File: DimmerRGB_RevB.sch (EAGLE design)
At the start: 54 parts, among them CON3 CON_10X200MIL, IC2 LM5111, IC3 LM2931_ADJ, IC4 LM5111, IC5 74HC14D, IC6 PIC16F18325, Q1 N-PWR-MOSFETLFPAK, Q2 N-PWR-MOSFETLFPAK, Q3 N-PWR-MOSFETLFPAK, Q4 N-PWR-MOSFETLFPAK, SW1 ENCODER_BOURNS, SW2 ENCODER_BOURNS, X1 22-23-2051

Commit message: Worked on RBG RevB layout
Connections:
- removed net N$16: R11.1, R12.1, SW2G$1.B, SW4G$1.B
- new net N$20: R11.1, R12.1, SW2G$1.B, SW4G$1.A
- net GND: now also SW3G$2.1, SW4G$2.1; no longer SW3G$2.2, SW4G$2.2
- net N$12: now also SW4G$2.2; no longer SW4G$2.1
- net N$13: now also SW3G$1.A; no longer SW3G$1.B
- net N$14: now also SW3G$1.B; no longer SW3G$1.A
- net N$17: now also SW4G$1.B; no longer SW4G$1.A
- net N$19: now also SW3G$2.2; no longer SW3G$2.1
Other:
- moved on the sheet: SW3, SW4
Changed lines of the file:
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@@
 <instance part="D4" gate="G$1" x="104.14" y="71.12"/>
 <instance part="SW3" gate="G$1" x="63.5" y="114.3"/>
-<instance part="SW3" gate="G$2" x="121.92" y="116.84" rot="R90"/>
+<instance part="SW3" gate="G$2" x="121.92" y="116.84" rot="R270"/>
 <instance part="SW4" gate="G$1" x="63.5" y="60.96"/>
-<instance part="SW4" gate="G$2" x="121.92" y="63.5" rot="R90"/>
+<instance part="SW4" gate="G$2" x="121.92" y="63.5" rot="R270"/>
 <instance part="GND37" gate="1" x="63.5" y="53.34"/>
 <instance part="GND38" gate="1" x="121.92" y="53.34"/>
@@
 </segment>
 <segment>
-<pinref part="SW4" gate="G$2" pin="2"/>
-<pinref part="GND38" gate="1" pin="GND"/>
-<wire x1="121.92" y1="58.42" x2="121.92" y2="55.88" width="0.1524" layer="91"/>
-</segment>
-<segment>
-<pinref part="SW3" gate="G$2" pin="2"/>
-<pinref part="GND39" gate="1" pin="GND"/>
-<wire x1="121.92" y1="111.76" x2="121.92" y2="109.22" width="0.1524" layer="91"/>
-</segment>
-<segment>
 <pinref part="SW3" gate="G$1" pin="C"/>
 <pinref part="GND40" gate="1" pin="GND"/>
 <wire x1="63.5" y1="111.76" x2="63.5" y2="109.22" width="0.1524" layer="91"/>
+</segment>
+<segment>
+<pinref part="SW4" gate="G$2" pin="1"/>
+<pinref part="GND38" gate="1" pin="GND"/>
+<wire x1="121.92" y1="58.42" x2="121.92" y2="55.88" width="0.1524" layer="91"/>
+</segment>
+<segment>
+<pinref part="SW3" gate="G$2" pin="1"/>
+<pinref part="GND39" gate="1" pin="GND"/>
+<wire x1="121.92" y1="111.76" x2="121.92" y2="109.22" width="0.1524" layer="91"/>
 </segment>
 </net>
@@
 <wire x1="55.88" y1="137.16" x2="55.88" y2="134.62" width="0.1524" layer="91"/>
 <pinref part="R6" gate="G$1" pin="1"/>
-<wire x1="55.88" y1="134.62" x2="55.88" y2="127" width="0.1524" layer="91"/>
-<wire x1="55.88" y1="127" x2="55.88" y2="121.92" width="0.1524" layer="91"/>
+<wire x1="55.88" y1="134.62" x2="55.88" y2="124.46" width="0.1524" layer="91"/>
+<wire x1="55.88" y1="124.46" x2="55.88" y2="121.92" width="0.1524" layer="91"/>
 <wire x1="58.42" y1="134.62" x2="55.88" y2="134.62" width="0.1524" layer="91"/>
 <junction x="55.88" y="134.62"/>
-<pinref part="SW3" gate="G$1" pin="B"/>
-<wire x1="55.88" y1="127" x2="66.04" y2="127" width="0.1524" layer="91"/>
-<wire x1="66.04" y1="127" x2="66.04" y2="121.92" width="0.1524" layer="91"/>
-<junction x="55.88" y="127"/>
+<pinref part="SW3" gate="G$1" pin="A"/>
+<wire x1="60.96" y1="121.92" x2="60.96" y2="124.46" width="0.1524" layer="91"/>
+<wire x1="60.96" y1="124.46" x2="55.88" y2="124.46" width="0.1524" layer="91"/>
+<junction x="55.88" y="124.46"/>
 </segment>
 </net>
@@
 <wire x1="50.8" y1="137.16" x2="50.8" y2="134.62" width="0.1524" layer="91"/>
 <pinref part="R2" gate="G$1" pin="2"/>
-<wire x1="50.8" y1="134.62" x2="50.8" y2="124.46" width="0.1524" layer="91"/>
-<wire x1="50.8" y1="124.46" x2="50.8" y2="121.92" width="0.1524" layer="91"/>
+<wire x1="50.8" y1="134.62" x2="50.8" y2="127" width="0.1524" layer="91"/>
+<wire x1="50.8" y1="127" x2="50.8" y2="121.92" width="0.1524" layer="91"/>
 <wire x1="48.26" y1="134.62" x2="50.8" y2="134.62" width="0.1524" layer="91"/>
 <junction x="50.8" y="134.62"/>
-<pinref part="SW3" gate="G$1" pin="A"/>
-<wire x1="50.8" y1="124.46" x2="60.96" y2="124.46" width="0.1524" layer="91"/>
-<wire x1="60.96" y1="124.46" x2="60.96" y2="121.92" width="0.1524" layer="91"/>
-<junction x="50.8" y="124.46"/>
+<pinref part="SW3" gate="G$1" pin="B"/>
+<wire x1="50.8" y1="127" x2="66.04" y2="127" width="0.1524" layer="91"/>
+<wire x1="66.04" y1="127" x2="66.04" y2="121.92" width="0.1524" layer="91"/>
+<junction x="50.8" y="127"/>
 </segment>
 </net>
@@
 <wire x1="182.88" y1="73.66" x2="172.72" y2="73.66" width="0.1524" layer="91"/>
 <label x="172.72" y="73.66" size="1.778" layer="95"/>
-</segment>
-</net>
-<net name="N$16" class="0">
-<segment>
-<pinref part="R11" gate="G$1" pin="1"/>
-<pinref part="SW2" gate="G$1" pin="B"/>
-<wire x1="55.88" y1="83.82" x2="55.88" y2="81.28" width="0.1524" layer="91"/>
-<pinref part="R12" gate="G$1" pin="1"/>
-<wire x1="55.88" y1="81.28" x2="55.88" y2="73.66" width="0.1524" layer="91"/>
-<wire x1="55.88" y1="73.66" x2="55.88" y2="68.58" width="0.1524" layer="91"/>
-<wire x1="58.42" y1="81.28" x2="55.88" y2="81.28" width="0.1524" layer="91"/>
-<junction x="55.88" y="81.28"/>
-<pinref part="SW4" gate="G$1" pin="B"/>
-<wire x1="66.04" y1="68.58" x2="66.04" y2="73.66" width="0.1524" layer="91"/>
-<wire x1="66.04" y1="73.66" x2="55.88" y2="73.66" width="0.1524" layer="91"/>
-<junction x="55.88" y="73.66"/>
-</segment>
-</net>
-<net name="N$17" class="0">
-<segment>
-<pinref part="R9" gate="G$1" pin="1"/>
-<pinref part="SW2" gate="G$1" pin="A"/>
-<wire x1="50.8" y1="83.82" x2="50.8" y2="81.28" width="0.1524" layer="91"/>
-<pinref part="R10" gate="G$1" pin="2"/>
-<wire x1="50.8" y1="81.28" x2="50.8" y2="71.12" width="0.1524" layer="91"/>
-<wire x1="50.8" y1="71.12" x2="50.8" y2="68.58" width="0.1524" layer="91"/>
-<wire x1="48.26" y1="81.28" x2="50.8" y2="81.28" width="0.1524" layer="91"/>
-<junction x="50.8" y="81.28"/>
-<pinref part="SW4" gate="G$1" pin="A"/>
-<wire x1="60.96" y1="68.58" x2="60.96" y2="71.12" width="0.1524" layer="91"/>
-<wire x1="60.96" y1="71.12" x2="50.8" y2="71.12" width="0.1524" layer="91"/>
-<junction x="50.8" y="71.12"/>
 </segment>
 </net>
@@
 <wire x1="114.3" y1="71.12" x2="106.68" y2="71.12" width="0.1524" layer="91"/>
 <junction x="114.3" y="71.12"/>
-<pinref part="SW4" gate="G$2" pin="1"/>
 <wire x1="114.3" y1="71.12" x2="121.92" y2="71.12" width="0.1524" layer="91"/>
+<pinref part="SW4" gate="G$2" pin="2"/>
 <wire x1="121.92" y1="71.12" x2="121.92" y2="68.58" width="0.1524" layer="91"/>
 </segment>
@@
 <wire x1="106.68" y1="124.46" x2="114.3" y2="124.46" width="0.1524" layer="91"/>
 <junction x="114.3" y="124.46"/>
-<pinref part="SW3" gate="G$2" pin="1"/>
 <wire x1="114.3" y1="124.46" x2="121.92" y2="124.46" width="0.1524" layer="91"/>
-<wire x1="121.92" y1="124.46" x2="121.92" y2="121.92" width="0.1524" layer="91"/>
-</segment>
-</net>
+<pinref part="SW3" gate="G$2" pin="2"/>
+<wire x1="121.92" y1="121.92" x2="121.92" y2="124.46" width="0.1524" layer="91"/>
+</segment>
+</net>
+<net name="N$20" class="0">
+<segment>
+<pinref part="SW4" gate="G$1" pin="A"/>
+<wire x1="60.96" y1="68.58" x2="60.96" y2="71.12" width="0.1524" layer="91"/>
+<pinref part="R11" gate="G$1" pin="1"/>
+<pinref part="SW2" gate="G$1" pin="B"/>
+<wire x1="55.88" y1="83.82" x2="55.88" y2="81.28" width="0.1524" layer="91"/>
+<pinref part="R12" gate="G$1" pin="1"/>
+<wire x1="55.88" y1="81.28" x2="55.88" y2="71.12" width="0.1524" layer="91"/>
+<wire x1="55.88" y1="71.12" x2="55.88" y2="68.58" width="0.1524" layer="91"/>
+<wire x1="58.42" y1="81.28" x2="55.88" y2="81.28" width="0.1524" layer="91"/>
+<junction x="55.88" y="81.28"/>
+<wire x1="60.96" y1="71.12" x2="55.88" y2="71.12" width="0.1524" layer="91"/>
+<junction x="55.88" y="71.12"/>
+</segment>
+</net>
+<net name="N$17" class="0">
+<segment>
+<pinref part="SW4" gate="G$1" pin="B"/>
+<wire x1="66.04" y1="68.58" x2="66.04" y2="73.66" width="0.1524" layer="91"/>
+<pinref part="R9" gate="G$1" pin="1"/>
+<pinref part="SW2" gate="G$1" pin="A"/>
+<wire x1="50.8" y1="83.82" x2="50.8" y2="81.28" width="0.1524" layer="91"/>
+<pinref part="R10" gate="G$1" pin="2"/>
+<wire x1="50.8" y1="81.28" x2="50.8" y2="73.66" width="0.1524" layer="91"/>
+<wire x1="50.8" y1="73.66" x2="50.8" y2="68.58" width="0.1524" layer="91"/>
+<wire x1="48.26" y1="81.28" x2="50.8" y2="81.28" width="0.1524" layer="91"/>
+<junction x="50.8" y="81.28"/>
+<wire x1="66.04" y1="73.66" x2="50.8" y2="73.66" width="0.1524" layer="91"/>
+<junction x="50.8" y="73.66"/>
+</segment>
+</net>

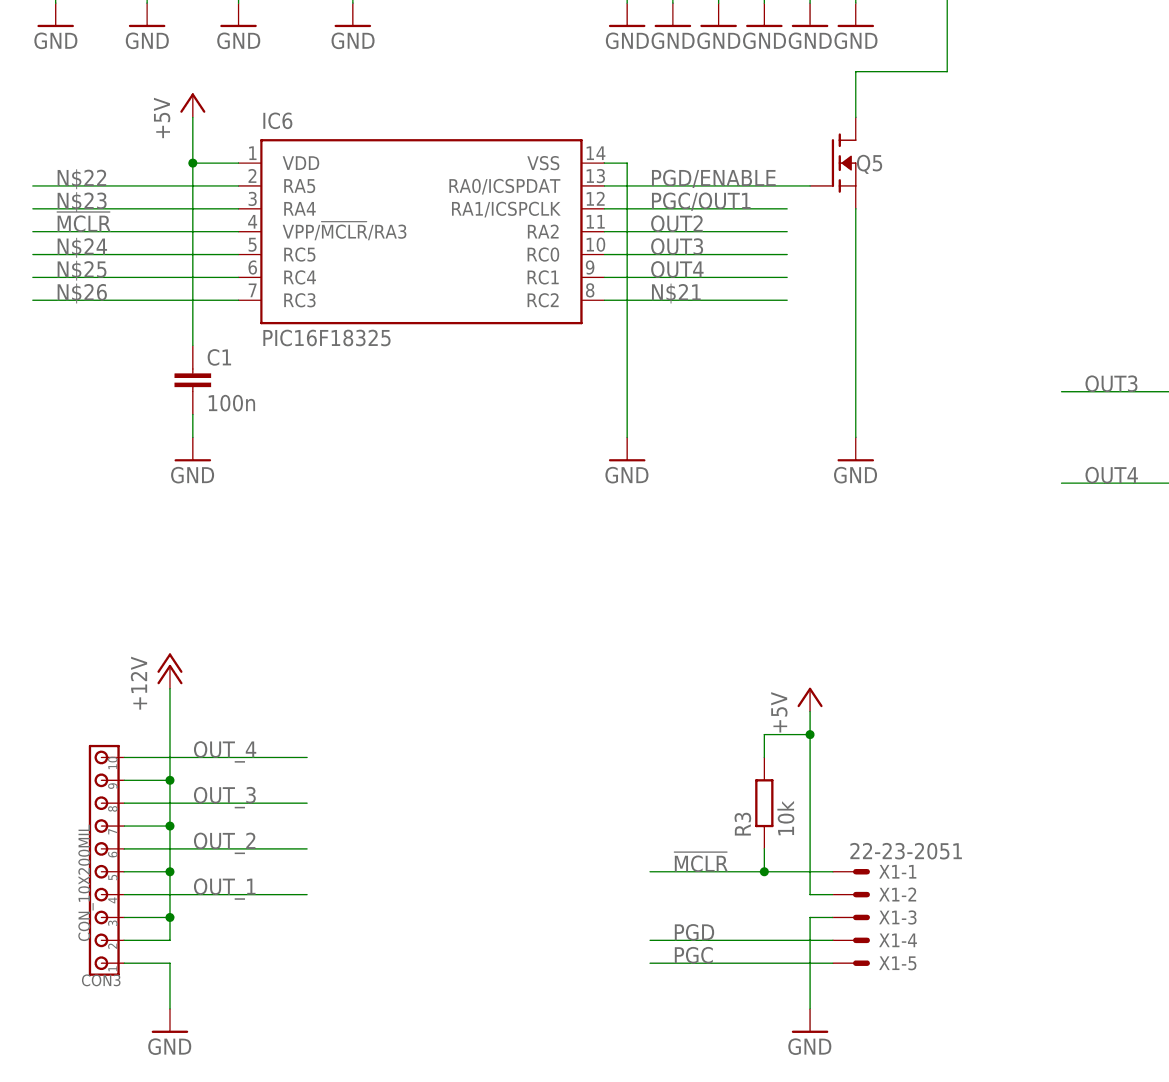
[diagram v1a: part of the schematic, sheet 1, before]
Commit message: Some more layouting done
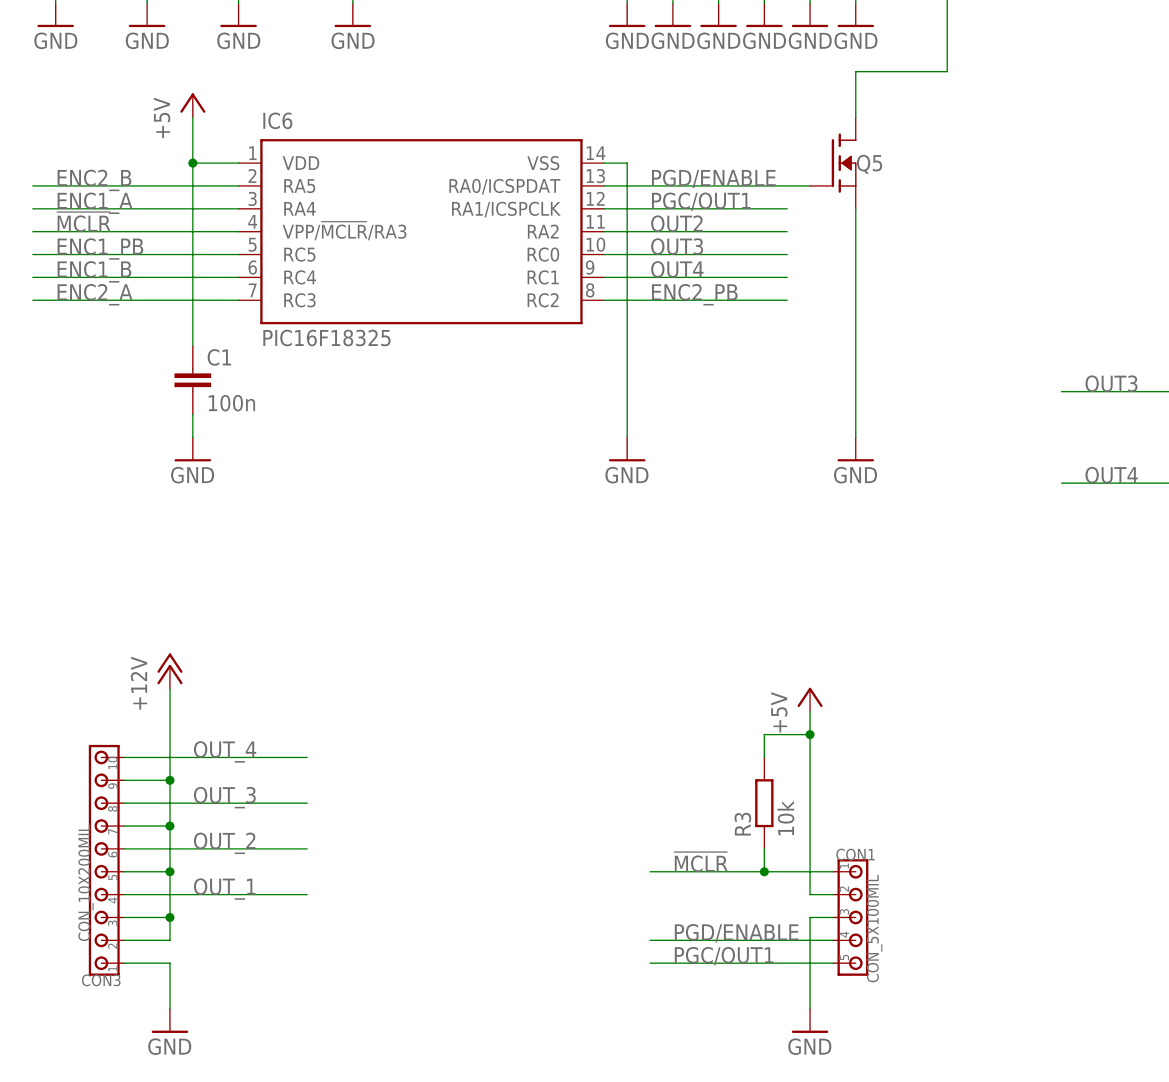
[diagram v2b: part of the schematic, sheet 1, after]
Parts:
- removed X1: 22-23-2051, 00Connector:22-23-2051
- added CON1: CON_5X100MIL, 00Connector:CON_5X100MIL
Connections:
- removed net N$21: IC6.RC2
- removed net N$22: IC6.RA5
- removed net N$23: IC6.RA4
- removed net N$24: IC6.RC5
- removed net N$25: IC6.RC4
- removed net N$26: IC6.RC3
- removed net PGC: X1-5.S
- removed net PGD: X1-4.S
- net !MCLR!: now also CON1.1; no longer X1-1.S
- net +5V: now also CON1.2; no longer X1-2.S
- net ENC1A: now also IC5.5A; no longer IC5.2A
- net ENC1B: now also IC5.6A; no longer IC5.3A
- net ENC1PB: now also IC5.4A; no longer IC5.1A
- net ENC1_A: now also IC5.5Y, IC6.RA4; no longer IC5.2Y
- net ENC1_B: now also IC5.6Y, IC6.RC4; no longer IC5.3Y
- net ENC1_PB: now also IC5.4Y, IC6.RC5; no longer IC5.1Y
- net ENC2A: now also IC5.1A; no longer IC5.5A
- net ENC2B: now also IC5.2A; no longer IC5.6A
- net ENC2PB: now also IC5.3A; no longer IC5.4A
- net ENC2_A: now also IC5.1Y, IC6.RC3; no longer IC5.5Y
- net ENC2_B: now also IC5.2Y, IC6.RA5; no longer IC5.6Y
- net ENC2_PB: now also IC5.3Y, IC6.RC2; no longer IC5.4Y
- net GND: now also CON1.3; no longer X1-3.S
- net PGC/OUT1: now also CON1.5
- net PGD/ENABLE: now also CON1.4

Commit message: Final version of RGB dimmer Rev B
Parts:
- removed CON3: CON_10X200MIL, 00Connector:CON_10X200MIL
- added C19, C20, C21, C22, C23, C8: 100n, 00Capacitor:CC0805
- added C7: 1500u, 00Capacitor:C_POLARIZED10MM
- added CON2: CON_5X100MIL, 00Connector:CON_5X100MIL
- C1: value 100n -> 33u; device 00Capacitor:CC0805 -> 00Capacitor:C_POLARIZEDSMC_C
- C11, C12: value 10n -> 100n
- C13, C14: value 100n -> 10n
- C17, C18, C2: value 1500u -> 100n; device 00Capacitor:C_POLARIZED10MM -> 00Capacitor:CC0805
- C3: value 33u -> 1500u; device 00Capacitor:C_POLARIZEDSMC_C -> 00Capacitor:C_POLARIZED10MM
- C6: value 100n -> 1500u; device 00Capacitor:CC0805 -> 00Capacitor:C_POLARIZED10MM
- CON1: value CON_5X100MIL -> CON_10X200MIL; device 00Connector:CON_5X100MIL -> 00Connector:CON_10X200MIL
- IC2: value LM5111 -> LM2931_ADJ; device 00Logic:LM5111 -> 00VoltageRegulator:LM2931_ADJ
- IC3: value LM2931_ADJ -> LM5111; device 00VoltageRegulator:LM2931_ADJ -> 00Logic:LM5111
- Q1: value N-PWR-MOSFETLFPAK -> (none); device 00Mosfet:N-PWR-MOSFETLFPAK -> 00Mosfet:N-FETSOT23
- Q5: value (none) -> N-PWR-MOSFETLFPAK; device 00Mosfet:N-FETSOT23 -> 00Mosfet:N-PWR-MOSFETLFPAK
- R1: value 10k -> 1k
- R10, R14, R8: value 22k -> 10k
- R13, R17, R7: value 10k -> 22k
- R15: value 33k -> 10k
- R16: value 33k -> 22k
- R2: value 22k -> 33k
- R4: value 1k -> 10k
- R5: value 10k -> 33k
- SW1, SW2: value ENCODER_BOURNS -> PEC11R
- SW3, SW4: value (none) -> PEC09
- renumbered IC6 to IC1
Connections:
- removed net N$6 (its old number): IC2.OUT_A, Q2.G
- new net N$5: IC3.OUT_A, Q2.G
- net !ENABLE!: now also D1.A, IC2.!EN!, Q1.D, R5.1; no longer D4.A, IC3.!EN!, Q5.D, R15.1
- net !MCLR!: now also CON2.1, R4.1; no longer CON1.1, R3.1
- net +12V: now also C3.+, C6.+, C7.+, C8.1, CON1.P$2, CON1.P$3, CON1.P$5, CON1.P$7, CON1.P$9, IC2.VIN, R5.2; no longer C17.+, C18.+, C2.+, CON3.P$2, CON3.P$3, CON3.P$5, CON3.P$7, CON3.P$9, IC3.VIN, R15.2
- net +5V: now also C1.+, C11.1, C12.1, C19.1, C2.1, C20.1, C21.1, C22.1, C23.1, C9.1, CON2.2, IC2.VOUT, IC3.VCC, R10.2, R14.2, R15.2, R2.2, R8.2; no longer C1.1, C13.1, C3.+, C6.1, CON1.2, IC2.VCC, IC3.VOUT, R13.2, R16.2, R3.2, R5.2, R7.2
- net ENC1A: now also C13.1, R6.1; no longer C11.1, R2.1
- net ENC1B: now also C15.1, R12.2; no longer C12.1, R6.2
- net ENC1PB: now also C17.1, R16.2; no longer C9.1, R8.2
- net ENC2A: now also C14.1, R7.1; no longer C15.1, R10.1
- net ENC2B: now also R13.2; no longer R12.2
- net ENC2PB: now also C18.1, R17.2; no longer C14.1, R14.2
- net GND: now also C1.-, C17.2, C18.2, C19.2, C2.2, C20.2, C21.2, C22.2, C23.2, C6.-, C7.-, C8.2, CON1.P$1, CON2.3, IC2.GND@1, IC2.GND@2, IC2.GND@3, IC2.GND@4, IC3.GND, R3.1; no longer C1.2, C17.-, C18.-, C2.-, C6.2, CON1.3, CON3.P$1, IC2.GND, IC3.GND@1, IC3.GND@2, IC3.GND@3, IC3.GND@4, R17.1
- net N$1: now also IC4.OUT_B, Q5.G; no longer IC2.OUT_B, Q1.G
- net N$11: now also IC3.OUT_B; no longer IC4.OUT_B
- net N$12: now also D2.C; no longer D3.C
- net N$13: now also R10.1, R12.1; no longer R5.1, R6.1
- net N$14: now also R6.2, R8.1; no longer R1.1, R2.2
- net N$15: now also D3.A, R14.1, R16.1; no longer D1.A, R7.1, R8.1
- net N$17: now also R7.2; no longer R10.2
- net N$18: now also D4.A, R15.1, R17.1; no longer D3.A, R13.1, R14.1
- net N$19: now also D3.C; no longer D2.C
- net N$2: now also R1.1; no longer R4.1
- net N$20: now also R13.1; no longer R12.1
- net N$8: now also IC2.ADJ, R2.1, R3.2; no longer IC3.ADJ, R16.1, R17.2
- net OUT2: now also IC3.IN_B; no longer IC4.IN_B
- net OUT3: now also IC4.IN_A; no longer IC2.IN_A
- net OUT4: now also IC4.IN_B; no longer IC2.IN_B
- net OUT_1: now also CON1.P$4, Q2.D; no longer CON3.P$4, Q4.D
- net OUT_2: now also CON1.P$6; no longer CON3.P$6
- net OUT_3: now also CON1.P$8, Q4.D; no longer CON3.P$8, Q2.D
- net OUT_4: now also CON1.P$10, Q5.D; no longer CON3.P$10, Q1.D
- net PGC/OUT1: now also CON2.5, IC3.IN_A; no longer CON1.5, IC4.IN_A
- net PGD/ENABLE: now also CON2.4, Q1.G; no longer CON1.4, Q5.G
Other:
- moved on the sheet: C10, C13, C14, C15, C3, C4, D1, D2, D3, D4, IC2, IC3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
